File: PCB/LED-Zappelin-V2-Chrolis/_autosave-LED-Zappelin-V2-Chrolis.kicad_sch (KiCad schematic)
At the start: 33 parts, among them J1 Blanking Signal, J2 Trigger, J3 Chrolis 1, J4 Chrolis 2, J5 NeoPixel Strip, J6 Barrel_Jack, Q1 2N5089, Q2 2N5089, SW1 Blanking Switch, SW2 Blanking Inverter Switch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

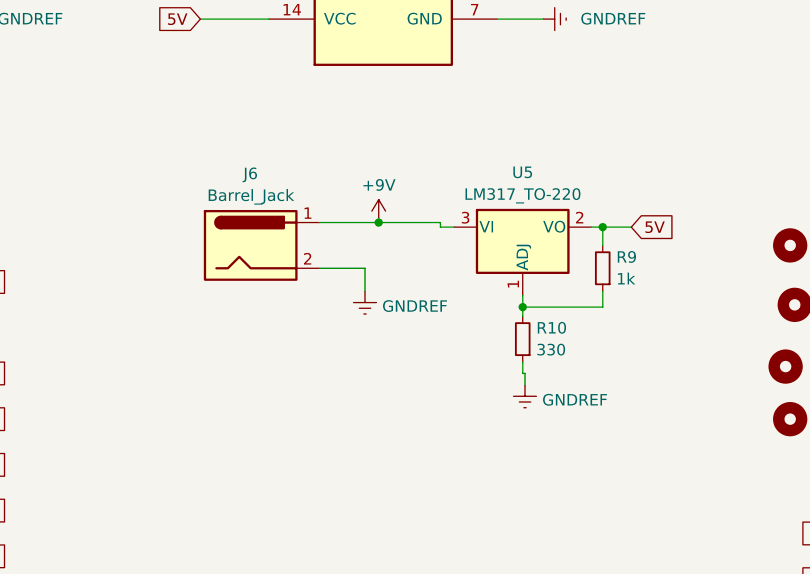
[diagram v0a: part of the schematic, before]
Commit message: update PCB
Previous modifications were kept, transistor Q2 was rerouted to sw1 pin6, all power line are now linked to external 5v power supply.
PCB was rearranged to accommodate box equipment. The neopixel strip for example requires 110mm +some tolerance on one side
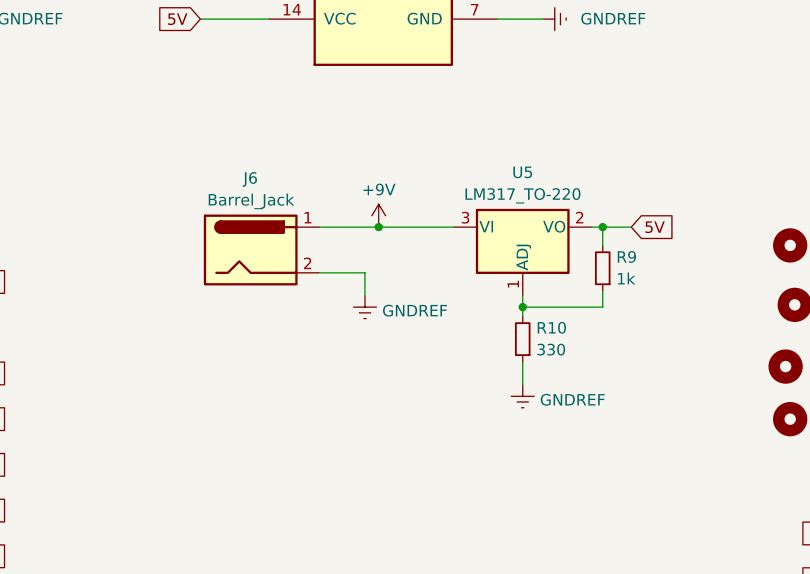
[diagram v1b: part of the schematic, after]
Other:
- moved on the sheet: J6
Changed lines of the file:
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@@
   (junction (at 247.65 73.66) (diameter 0) (color 0 0 0 0)
   )
-  (junction (at 173.482 92.456) (diameter 0) (color 0 0 0 0)
+  (junction (at 173.482 92.964) (diameter 0) (color 0 0 0 0)
   )
   (junction (at 247.65 63.5) (diameter 0) (color 0 0 0 0)
@@
     (stroke (width 0) (type default))
   )
-  (wire (pts (xy 173.482 92.456) (xy 180.34 92.456))
+  (wire (pts (xy 173.482 92.964) (xy 181.864 92.964))
     (stroke (width 0) (type default))
   )
@@
     (stroke (width 0) (type default))
   )
-  (wire (pts (xy 166.878 92.456) (xy 173.482 92.456))
+  (wire (pts (xy 166.878 92.964) (xy 173.482 92.964))
     (stroke (width 0) (type default))
   )
@@
     (stroke (width 0) (type default))
   )
-  (wire (pts (xy 171.958 100.076) (xy 171.958 97.536))
+  (wire (pts (xy 171.958 100.584) (xy 171.958 98.044))
     (stroke (width 0) (type default))
   )
@@
     (stroke (width 0) (type default))
   )
-  (wire (pts (xy 189.738 109.22) (xy 189.738 110.49))
-    (stroke (width 0) (type default))
-  )
   (wire (pts (xy 154.94 185.42) (xy 149.86 185.42))
     (stroke (width 0) (type default))
@@
     (stroke (width 0) (type default))
   )
-  (wire (pts (xy 189.484 107.95) (xy 189.484 109.22))
+  (wire (pts (xy 189.484 107.95) (xy 189.484 110.49))
     (stroke (width 0) (type default))
   )
@@
     (stroke (width 0) (type default))
   )
-  (wire (pts (xy 189.484 109.22) (xy 189.738 109.22))
-    (stroke (width 0) (type default))
-  )
   (wire (pts (xy 234.95 45.72) (xy 260.35 45.72))
     (stroke (width 0) (type default))
@@
     (stroke (width 0) (type default))
   )
-  (wire (pts (xy 180.34 92.964) (xy 181.864 92.964))
-    (stroke (width 0) (type default))
-  )
   (wire (pts (xy 247.65 43.18) (xy 260.35 43.18))
     (stroke (width 0) (type default))
@@
     (stroke (width 0) (type default))
   )
-  (wire (pts (xy 180.34 92.456) (xy 180.34 92.964))
-    (stroke (width 0) (type default))
-  )
   (wire (pts (xy 247.65 43.18) (xy 247.65 48.26))
     (stroke (width 0) (type default))
@@
     (stroke (width 0) (type default))
   )
-  (wire (pts (xy 171.958 97.536) (xy 166.878 97.536))
+  (wire (pts (xy 171.958 98.044) (xy 166.878 98.044))
     (stroke (width 0) (type default))
   )
@@
     )
   )
-  (symbol (lib_id "power:GNDREF") (at 189.738 110.49 0) (unit 1)
+  (symbol (lib_id "power:GNDREF") (at 189.484 110.49 0) (unit 1)
     (in_bom yes) (on_board yes) (dnp no) (fields_autoplaced)
-    (property "Reference" "#PWR03" (at 189.738 116.84 0)
-      (effects (font (size 1.27 1.27)) hide)
-    )
-    (property "Value" "GNDREF" (at 191.643 112.1938 0)
+    (property "Reference" "#PWR03" (at 189.484 116.84 0)
+      (effects (font (size 1.27 1.27)) hide)
+    )
+    (property "Value" "GNDREF" (at 191.389 112.1938 0)
       (effects (font (size 1.27 1.27)) (justify left))
     )
-    (property "Footprint" "" (at 189.738 110.49 0)
-      (effects (font (size 1.27 1.27)) hide)
-    )
-    (property "Datasheet" "" (at 189.738 110.49 0)
+    (property "Footprint" "" (at 189.484 110.49 0)
+      (effects (font (size 1.27 1.27)) hide)
+    )
+    (property "Datasheet" "" (at 189.484 110.49 0)
       (effects (font (size 1.27 1.27)) hide)
     )
@@
     )
   )
-  (symbol (lib_id "power:GNDREF") (at 171.958 100.076 0) (unit 1)
+  (symbol (lib_id "power:GNDREF") (at 171.958 100.584 0) (unit 1)
     (in_bom yes) (on_board yes) (dnp no) (fields_autoplaced)
-    (property "Reference" "#PWR01" (at 171.958 106.426 0)
-      (effects (font (size 1.27 1.27)) hide)
-    )
-    (property "Value" "GNDREF" (at 173.863 101.7798 0)
+    (property "Reference" "#PWR01" (at 171.958 106.934 0)
+      (effects (font (size 1.27 1.27)) hide)
+    )
+    (property "Value" "GNDREF" (at 173.863 102.2878 0)
       (effects (font (size 1.27 1.27)) (justify left))
     )
-    (property "Footprint" "" (at 171.958 100.076 0)
-      (effects (font (size 1.27 1.27)) hide)
-    )
-    (property "Datasheet" "" (at 171.958 100.076 0)
+    (property "Footprint" "" (at 171.958 100.584 0)
+      (effects (font (size 1.27 1.27)) hide)
+    )
+    (property "Datasheet" "" (at 171.958 100.584 0)
       (effects (font (size 1.27 1.27)) hide)
     )
@@
     )
   )
-  (symbol (lib_id "Connector:Barrel_Jack") (at 159.258 94.996 0) (unit 1)
+  (symbol (lib_id "Connector:Barrel_Jack") (at 159.258 95.504 0) (unit 1)
     (in_bom yes) (on_board yes) (dnp no) (fields_autoplaced)
-    (property "Reference" "J6" (at 159.258 87.0417 0)
-      (effects (font (size 1.27 1.27)))
-    )
-    (property "Value" "Barrel_Jack" (at 159.258 89.4659 0)
-      (effects (font (size 1.27 1.27)))
-    )
-    (property "Footprint" "Connector_BarrelJack:BarrelJack_Horizontal" (at 160.528 96.012 0)
-      (effects (font (size 1.27 1.27)) hide)
-    )
-    (property "Datasheet" "~" (at 160.528 96.012 0)
+    (property "Reference" "J6" (at 159.258 87.5497 0)
+      (effects (font (size 1.27 1.27)))
+    )
+    (property "Value" "Barrel_Jack" (at 159.258 89.9739 0)
+      (effects (font (size 1.27 1.27)))
+    )
+    (property "Footprint" "Connector_BarrelJack:BarrelJack_Horizontal" (at 160.528 96.52 0)
+      (effects (font (size 1.27 1.27)) hide)
+    )
+    (property "Datasheet" "~" (at 160.528 96.52 0)
       (effects (font (size 1.27 1.27)) hide)
     )
@@
     )
   )
-  (symbol (lib_id "power:+9V") (at 173.482 92.456 0) (unit 1)
+  (symbol (lib_id "power:+9V") (at 173.482 92.964 0) (unit 1)
     (in_bom yes) (on_board yes) (dnp no) (fields_autoplaced)
-    (property "Reference" "#PWR02" (at 173.482 96.266 0)
-      (effects (font (size 1.27 1.27)) hide)
-    )
-    (property "Value" "+9V" (at 173.482 88.3229 0)
-      (effects (font (size 1.27 1.27)))
-    )
-    (property "Footprint" "" (at 173.482 92.456 0)
-      (effects (font (size 1.27 1.27)) hide)
-    )
-    (property "Datasheet" "" (at 173.482 92.456 0)
-      (effects (font (size 1.27 1.27)) hide)
-    )
+    (property "Reference" "#PWR02" (at 173.482 96.774 0)
+      (effects (font (size 1.27 1.27)) hide)
+    )
+    (property "Value" "+9V" (at 173.482 88.8309 0)
+      (effects (font (size 1.27 1.27)))
+    )
+    (property "Footprint" "" (at 173.482 92.964 0)
+      (effects (font (size 1.27 1.27)) hide)
+    )
+    (property "Datasheet" "" (at 173.482 92.964 0)
+      (effects (font (size 1.27 1.27)) hide)
+    )
